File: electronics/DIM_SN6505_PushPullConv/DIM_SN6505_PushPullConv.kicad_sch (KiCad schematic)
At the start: 18 parts, among them J1 Conn_01x04, J2 Conn_01x04, J3 Conn_01x04, J4 Conn_01x04, T1 STR7040, U1 SN6506A

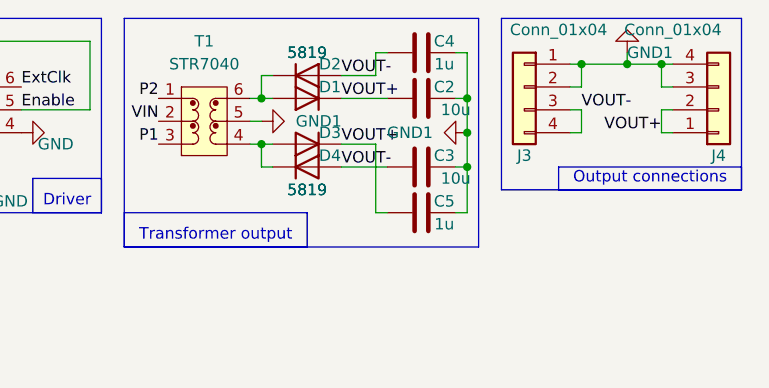
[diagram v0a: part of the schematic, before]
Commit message: renamed and cleaned up SN6505 breakout
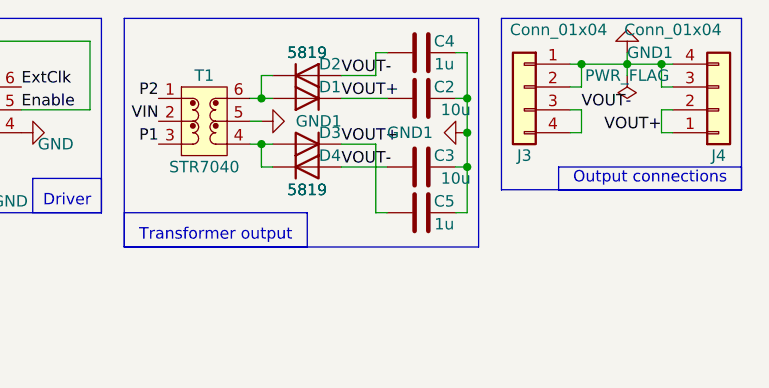
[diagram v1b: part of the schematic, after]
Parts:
- T1: symbol SquantorVPSC:T_6pin -> SquantorTransformer:PushPull_6pin
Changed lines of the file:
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@@
+	(wire
+		(pts
+			(xy 132.08 20.32) (xy 132.08 21.59)
+		)
+		(stroke
+			(width 0)
+			(type default)
+		)
+	)
 	(wire
 		(pts
@@
 	)
 	(symbol
-		(lib_id "SquantorVPSC:T_6pin")
+		(lib_id "SquantorTransformer:PushPull_6pin")
 		(at 85.09 26.67 0)
 		(unit 1)
@@
 		(on_board yes)
 		(dnp no)
-		(fields_autoplaced yes)
 		(property "Reference" "T1"
-			(at 85.09 17.78 0)
+			(at 85.09 21.59 0)
 			(effects
 				(font
@@
 		)
 		(property "Value" "STR7040"
-			(at 85.09 20.32 0)
+			(at 85.09 31.75 0)
 			(effects
 				(font
@@
 					(unit 1)
 				)
+			)
+		)
+	)
+	(symbol
+		(lib_id "power:PWR_FLAG")
+		(at 132.08 21.59 180)
+		(unit 1)
+		(exclude_from_sim no)
+		(in_bom yes)
+		(on_board yes)
+		(dnp no)
+		(property "Reference" "#FLG03"
+			(at 132.08 23.495 0)
+			(effects
+				(font
+					(size 1.27 1.27)
+				)
+				(hide yes)
+			)
+		)
+		(property "Value" "PWR_FLAG"
+			(at 132.08 21.59 0)
+			(effects
+				(font
+					(size 1.27 1.27)
+				)
+			)
+		)
+		(property "Footprint" ""
+			(at 132.08 21.59 0)
+			(effects
+				(font
+					(size 1.27 1.27)
+				)
+				(hide yes)
+			)
+		)
+		(property "Datasheet" "~"
+			(at 132.08 21.59 0)
+			(effects
+				(font
+					(size 1.27 1.27)
+				)
+				(hide yes)
+			)
+		)
+		(property "Description" "Special symbol for telling ERC where power comes from"
+			(at 132.08 21.59 0)
+			(effects
+				(font
+					(size 1.27 1.27)
+				)
+				(hide yes)
+			)
+		)
+		(pin "1"
+		)
+		(instances
+			(project "DIM_SN6505_PushPullConv"
+				(path "/646d9e91-59b4-4865-a2fc-29780ed32563"
+					(reference "#FLG03")
+					(unit 1)
+				)

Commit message: preparation for production V20260118
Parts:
- N1: value 20251002 -> 20260118
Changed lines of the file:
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@@
 			)
 		)
-		(property "Value" "20251002"
+		(property "Value" "20260118"
 			(at 20.32 189.23 0)
 			(effects
